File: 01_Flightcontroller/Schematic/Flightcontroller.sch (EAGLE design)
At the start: 86 parts, among them IC1 FT232RL, IC2 MPU6000, IC3 BMP280, J1 2908-05WB-MG, U1 STM32F7X2RXT, U2 ATMEGA328P_TQFP, U3 LM3940IMPX-3.3/NOPB, U4 TXB0104, Y1 8MHz, Y2 16MHz

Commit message: Hinzufügen STNUCLEO144_MANUAL.pdf
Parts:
- renumbered JP1 to ADC1, JP2 to ADC2, JP3 to GY87, JP4 to JTAG
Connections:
- removed net CS: U1A.PC6
- net CE: now also U1A.PC6
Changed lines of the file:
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@@
 <part name="GND21" library="SparkFun-PowerSymbols" library_urn="urn:adsk.eagle:library:530" deviceset="GND" device=""/>
 <part name="C31" library="rcl" library_urn="urn:adsk.eagle:library:334" deviceset="C-EU" device="C1206" package3d_urn="urn:adsk.eagle:package:23618/2" value="100nF"/>
-<part name="JP1" library="adafruit" library_urn="urn:adsk.eagle:library:420" deviceset="PINHD-1X3" device="" package3d_urn="urn:adsk.eagle:package:6240710/1"/>
-<part name="JP2" library="adafruit" library_urn="urn:adsk.eagle:library:420" deviceset="PINHD-1X3" device="" package3d_urn="urn:adsk.eagle:package:6240710/1"/>
+<part name="ADC1" library="adafruit" library_urn="urn:adsk.eagle:library:420" deviceset="PINHD-1X3" device="" package3d_urn="urn:adsk.eagle:package:6240710/1"/>
+<part name="ADC2" library="adafruit" library_urn="urn:adsk.eagle:library:420" deviceset="PINHD-1X3" device="" package3d_urn="urn:adsk.eagle:package:6240710/1"/>
 <part name="GND22" library="SparkFun-PowerSymbols" library_urn="urn:adsk.eagle:library:530" deviceset="GND" device=""/>
 <part name="SUPPLY23" library="SparkFun-PowerSymbols" library_urn="urn:adsk.eagle:library:530" deviceset="VCC_2" device=""/>
@@
 <part name="GND24" library="SparkFun-PowerSymbols" library_urn="urn:adsk.eagle:library:530" deviceset="GND" device=""/>
 <part name="SUPPLY25" library="SparkFun-PowerSymbols" library_urn="urn:adsk.eagle:library:530" deviceset="VCC" device=""/>
-<part name="JP3" library="adafruit" library_urn="urn:adsk.eagle:library:420" deviceset="PINHD-1X8" device="CLEANBIG" package3d_urn="urn:adsk.eagle:package:6240708/1"/>
+<part name="GY87" library="adafruit" library_urn="urn:adsk.eagle:library:420" deviceset="PINHD-1X8" device="CLEANBIG" package3d_urn="urn:adsk.eagle:package:6240708/1"/>
 <part name="GND25" library="SparkFun-PowerSymbols" library_urn="urn:adsk.eagle:library:530" deviceset="GND" device=""/>
 <part name="SUPPLY26" library="SparkFun-PowerSymbols" library_urn="urn:adsk.eagle:library:530" deviceset="VCC" device=""/>
-<part name="JP4" library="adafruit" library_urn="urn:adsk.eagle:library:420" deviceset="PINHD-1X6" device="" package3d_urn="urn:adsk.eagle:package:6240711/1"/>
+<part name="JTAG" library="adafruit" library_urn="urn:adsk.eagle:library:420" deviceset="PINHD-1X6" device="" package3d_urn="urn:adsk.eagle:package:6240711/1"/>
 <part name="GND26" library="SparkFun-PowerSymbols" library_urn="urn:adsk.eagle:library:530" deviceset="GND" device=""/>
 <part name="SUPPLY27" library="SparkFun-PowerSymbols" library_urn="urn:adsk.eagle:library:530" deviceset="VCC" device=""/>
@@
 <attribute name="VALUE" x="98.171" y="6.096" size="1.778" layer="96" rot="R270"/>
 </instance>
-<instance part="JP1" gate="A" x="373.38" y="-63.5" smashed="yes">
+<instance part="ADC1" gate="A" x="373.38" y="-63.5" smashed="yes">
 <attribute name="NAME" x="367.03" y="-57.785" size="1.778" layer="95"/>
 <attribute name="VALUE" x="367.03" y="-71.12" size="1.778" layer="96"/>
 </instance>
-<instance part="JP2" gate="A" x="373.38" y="-78.74" smashed="yes">
+<instance part="ADC2" gate="A" x="373.38" y="-78.74" smashed="yes">
 <attribute name="NAME" x="367.03" y="-73.025" size="1.778" layer="95"/>
 <attribute name="VALUE" x="367.03" y="-86.36" size="1.778" layer="96"/>
@@
 <attribute name="VALUE" x="-48.26" y="-21.336" size="1.778" layer="96" align="bottom-center"/>
 </instance>
-<instance part="JP3" gate="G$1" x="173.99" y="-91.44" smashed="yes" rot="R180">
+<instance part="GY87" gate="G$1" x="173.99" y="-91.44" smashed="yes" rot="R180">
 <attribute name="NAME" x="180.34" y="-102.235" size="1.778" layer="95" rot="R180"/>
 <attribute name="VALUE" x="180.34" y="-76.2" size="1.778" layer="96" rot="R180"/>
@@
 <attribute name="VALUE" x="181.61" y="-70.866" size="1.778" layer="96" align="bottom-center"/>
 </instance>
-<instance part="JP4" gate="A" x="-5.08" y="-27.94" smashed="yes" rot="R180">
-<attribute name="NAME" x="1.27" y="-38.735" size="1.778" layer="95" rot="R180"/>
+<instance part="JTAG" gate="A" x="-5.08" y="-27.94" smashed="yes" rot="R180">
+<attribute name="NAME" x="2.54" y="-38.735" size="1.778" layer="95" rot="R180"/>
 <attribute name="VALUE" x="1.27" y="-17.78" size="1.778" layer="96" rot="R180"/>
 </instance>
@@
 </segment>
 <segment>
-<pinref part="JP1" gate="A" pin="3"/>
+<pinref part="ADC1" gate="A" pin="3"/>
 <wire x1="370.84" y1="-66.04" x2="364.49" y2="-66.04" width="0.1524" layer="91"/>
-<pinref part="JP2" gate="A" pin="3"/>
+<pinref part="ADC2" gate="A" pin="3"/>
 <wire x1="364.49" y1="-66.04" x2="364.49" y2="-81.28" width="0.1524" layer="91"/>
 <wire x1="364.49" y1="-81.28" x2="370.84" y2="-81.28" width="0.1524" layer="91"/>
@@
 </segment>
 <segment>
-<pinref part="JP3" gate="G$1" pin="6"/>
+<pinref part="GY87" gate="G$1" pin="6"/>
 <wire x1="176.53" y1="-86.36" x2="181.61" y2="-86.36" width="0.1524" layer="91"/>
 <wire x1="181.61" y1="-86.36" x2="181.61" y2="-106.68" width="0.1524" layer="91"/>
@@
 </segment>
 <segment>
-<pinref part="JP4" gate="A" pin="3"/>
+<pinref part="JTAG" gate="A" pin="3"/>
 <wire x1="-2.54" y1="-30.48" x2="-1.27" y2="-30.48" width="0.1524" layer="91"/>
 <wire x1="-1.27" y1="-30.48" x2="-1.27" y2="-43.18" width="0.1524" layer="91"/>
@@
 </segment>
 <segment>
-<pinref part="JP3" gate="G$1" pin="7"/>
+<pinref part="GY87" gate="G$1" pin="7"/>
 <wire x1="176.53" y1="-83.82" x2="181.61" y2="-83.82" width="0.1524" layer="91"/>
 <wire x1="181.61" y1="-83.82" x2="181.61" y2="-73.66" width="0.1524" layer="91"/>
@@
 </segment>
 <segment>
-<pinref part="JP4" gate="A" pin="1"/>
+<pinref part="JTAG" gate="A" pin="1"/>
 <wire x1="-2.54" y1="-35.56" x2="0" y2="-35.56" width="0.1524" layer="91"/>
 <wire x1="0" y1="-35.56" x2="0" y2="-15.24" width="0.1524" layer="91"/>
@@
 </segment>
 <segment>
-<pinref part="JP2" gate="A" pin="2"/>
+<pinref part="ADC2" gate="A" pin="2"/>
 <wire x1="370.84" y1="-78.74" x2="363.22" y2="-78.74" width="0.1524" layer="91"/>
 <wire x1="363.22" y1="-78.74" x2="363.22" y2="-63.5" width="0.1524" layer="91"/>
-<pinref part="JP1" gate="A" pin="2"/>
+<pinref part="ADC1" gate="A" pin="2"/>
 <wire x1="363.22" y1="-63.5" x2="370.84" y2="-63.5" width="0.1524" layer="91"/>
 <wire x1="363.22" y1="-63.5" x2="363.22" y2="-52.07" width="0.1524" layer="91"/>
@@
 </segment>
 <segment>
-<pinref part="JP4" gate="A" pin="4"/>
+<pinref part="JTAG" gate="A" pin="4"/>
 <wire x1="-2.54" y1="-27.94" x2="10.16" y2="-27.94" width="0.1524" layer="91"/>
 <label x="2.54" y="-27.94" size="1.778" layer="95"/>
@@
 </segment>
 <segment>
-<pinref part="JP4" gate="A" pin="2"/>
+<pinref part="JTAG" gate="A" pin="2"/>
 <wire x1="-2.54" y1="-33.02" x2="10.16" y2="-33.02" width="0.1524" layer="91"/>
 <label x="2.54" y="-33.02" size="1.778" layer="95"/>
@@
 </segment>
 <segment>
-<pinref part="JP4" gate="A" pin="6"/>
+<pinref part="JTAG" gate="A" pin="6"/>
 <wire x1="-2.54" y1="-22.86" x2="10.16" y2="-22.86" width="0.1524" layer="91"/>
 <label x="2.54" y="-22.86" size="1.778" layer="95"/>
@@
 </segment>
 <segment>
-<pinref part="JP3" gate="G$1" pin="4"/>
+<pinref part="GY87" gate="G$1" pin="4"/>
 <wire x1="176.53" y1="-91.44" x2="187.96" y2="-91.44" width="0.1524" layer="91"/>
 <label x="182.88" y="-91.44" size="1.778" layer="95"/>
@@
 </segment>
 <segment>
-<pinref part="JP3" gate="G$1" pin="5"/>
+<pinref part="GY87" gate="G$1" pin="5"/>
 <wire x1="176.53" y1="-88.9" x2="187.96" y2="-88.9" width="0.1524" layer="91"/>
 <label x="182.88" y="-88.9" size="1.778" layer="95"/>
@@
 <wire x1="-74.93" y1="0" x2="-81.28" y2="0" width="0.1524" layer="91"/>
 <label x="-80.01" y="0" size="1.778" layer="95"/>
+</segment>
+<segment>
+<pinref part="U1" gate="A" pin="PC6"/>
+<wire x1="68.58" y1="78.74" x2="72.39" y2="78.74" width="0.1524" layer="91"/>
+<label x="68.58" y="78.74" size="1.778" layer="95"/>
 </segment>
 </net>
@@
 </segment>
 <segment>
-<pinref part="JP4" gate="A" pin="5"/>
+<pinref part="JTAG" gate="A" pin="5"/>
 <wire x1="-2.54" y1="-25.4" x2="10.16" y2="-25.4" width="0.1524" layer="91"/>
 <label x="2.54" y="-25.4" size="1.778" layer="95"/>
@@
 </segment>
 <segment>
-<pinref part="JP1" gate="A" pin="1"/>
+<pinref part="ADC1" gate="A" pin="1"/>
 <wire x1="370.84" y1="-60.96" x2="360.68" y2="-60.96" width="0.1524" layer="91"/>
 <label x="360.68" y="-60.96" size="1.778" layer="95"/>
@@
 </segment>
 <segment>
-<pinref part="JP2" gate="A" pin="1"/>
+<pinref part="ADC2" gate="A" pin="1"/>
 <wire x1="370.84" y1="-76.2" x2="360.68" y2="-76.2" width="0.1524" layer="91"/>
 <label x="360.68" y="-76.2" size="1.778" layer="95"/>
-</segment>
-</net>
-<net name="CS" class="0">
-<segment>
-<pinref part="U1" gate="A" pin="PC6"/>
-<wire x1="68.58" y1="78.74" x2="72.39" y2="78.74" width="0.1524" layer="91"/>
-<label x="68.58" y="78.74" size="1.778" layer="95"/>
 </segment>
 </net>
@@
 <net name="FSYNC" class="0">
 <segment>
-<pinref part="JP3" gate="G$1" pin="3"/>
+<pinref part="GY87" gate="G$1" pin="3"/>
 <wire x1="176.53" y1="-93.98" x2="187.96" y2="-93.98" width="0.1524" layer="91"/>
 <label x="182.88" y="-93.98" size="1.778" layer="95"/>
@@
 <net name="INTA" class="0">
 <segment>
-<pinref part="JP3" gate="G$1" pin="2"/>
+<pinref part="GY87" gate="G$1" pin="2"/>
 <wire x1="176.53" y1="-96.52" x2="187.96" y2="-96.52" width="0.1524" layer="91"/>
 <label x="182.88" y="-96.52" size="1.778" layer="95"/>
@@
 <net name="DRDY" class="0">
 <segment>
-<pinref part="JP3" gate="G$1" pin="1"/>
+<pinref part="GY87" gate="G$1" pin="1"/>
 <wire x1="176.53" y1="-99.06" x2="187.96" y2="-99.06" width="0.1524" layer="91"/>
 <label x="182.88" y="-99.06" size="1.778" layer="95"/>

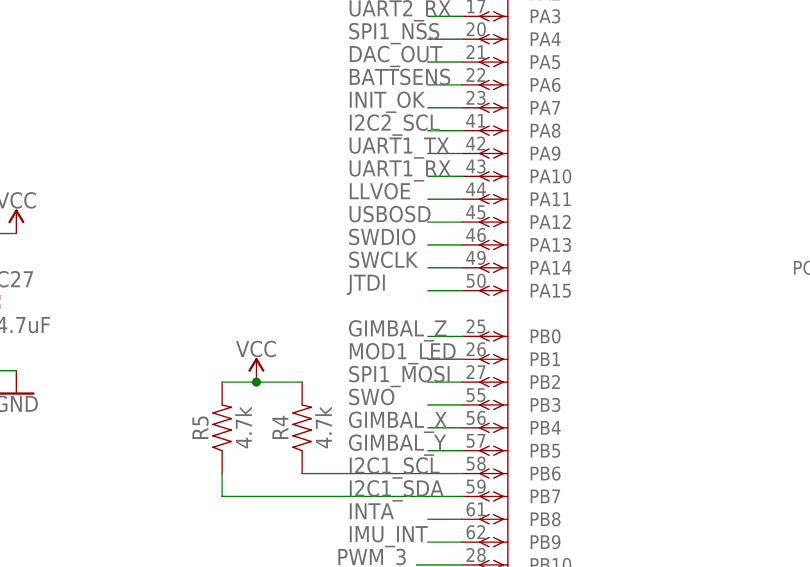
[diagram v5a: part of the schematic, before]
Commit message: JTAG -> Serial Wire
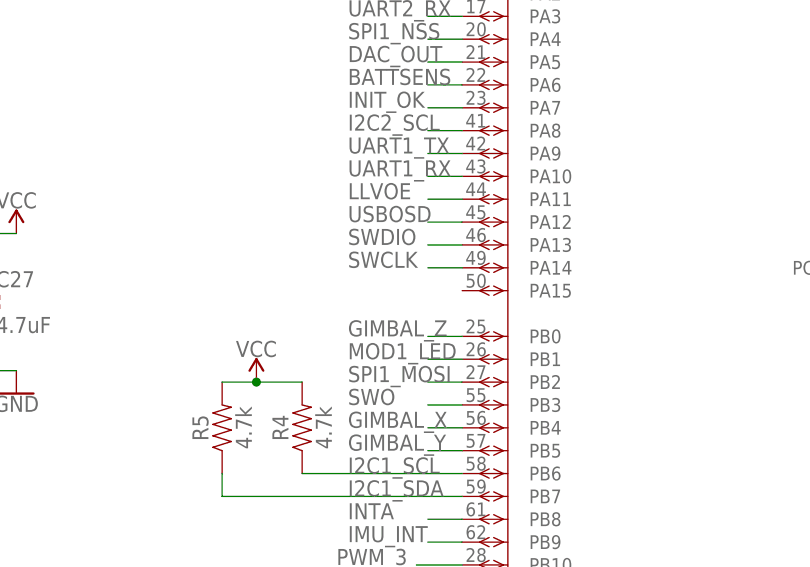
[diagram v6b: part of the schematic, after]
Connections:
- removed net JTDI: U1A.PA15
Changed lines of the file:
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@@
-</segment>
-</net>
-<net name="JTDI" class="0">
-<segment>
-<pinref part="U1" gate="A" pin="PA15"/>
-<wire x1="7.62" y1="53.34" x2="3.81" y2="53.34" width="0.1524" layer="91"/>
-<label x="-5.08" y="53.34" size="1.778" layer="95"/>
 </segment>
 </net>
